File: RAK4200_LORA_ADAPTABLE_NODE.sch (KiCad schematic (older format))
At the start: 7 parts, among them U1 RAK4200

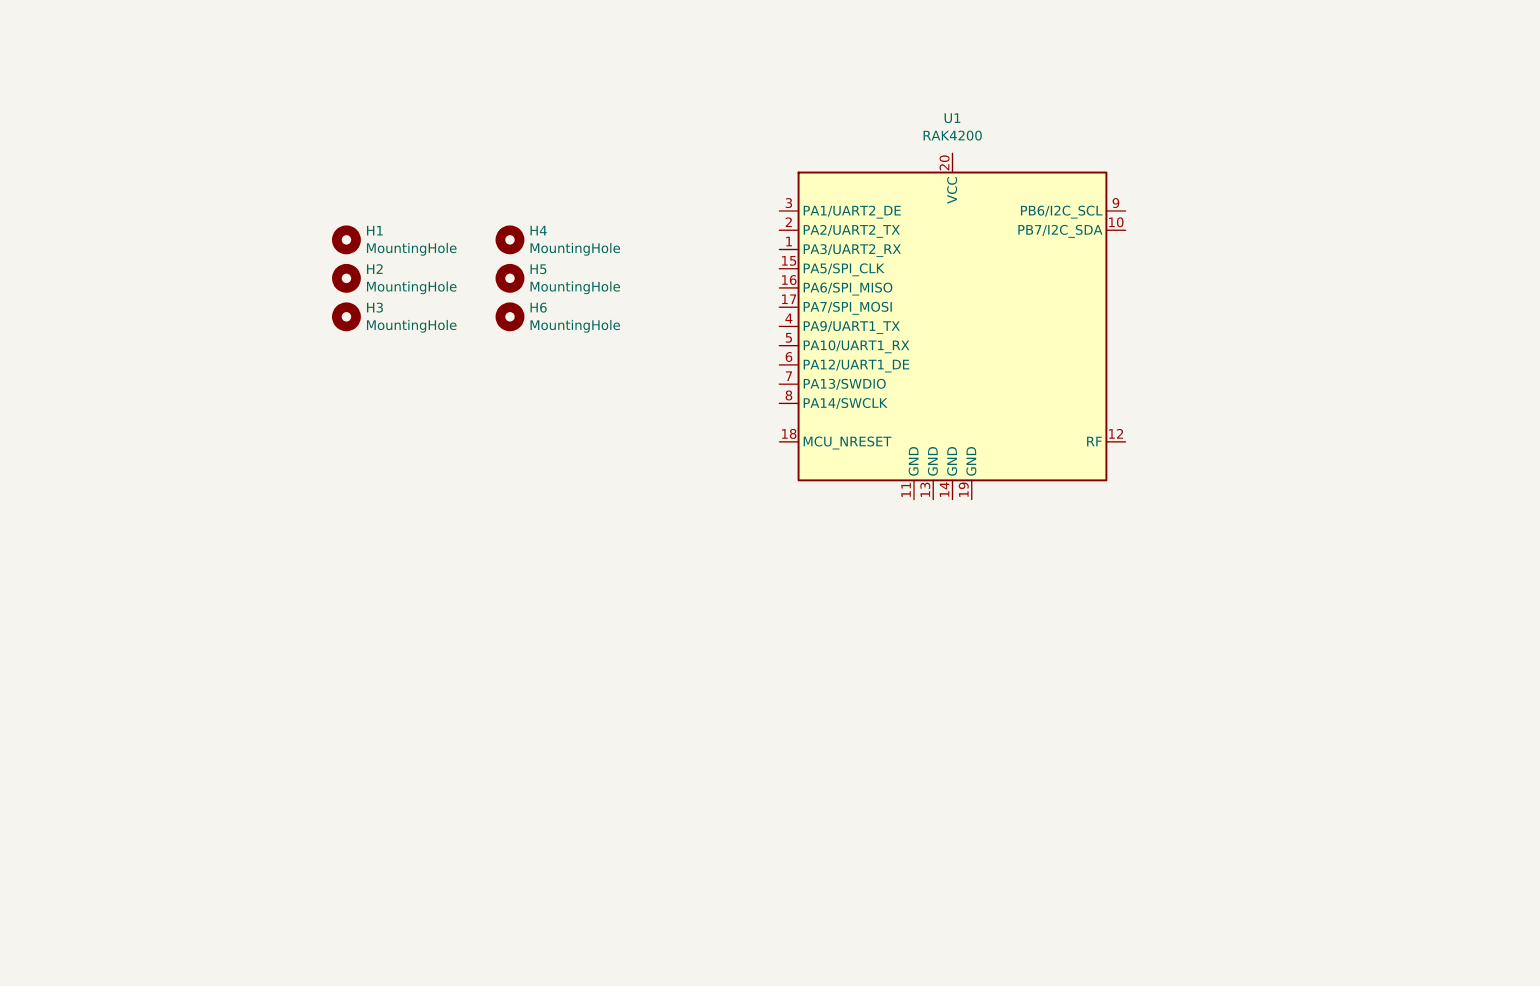
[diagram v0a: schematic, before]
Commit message: battery holder, solder jumper and screw terminal added
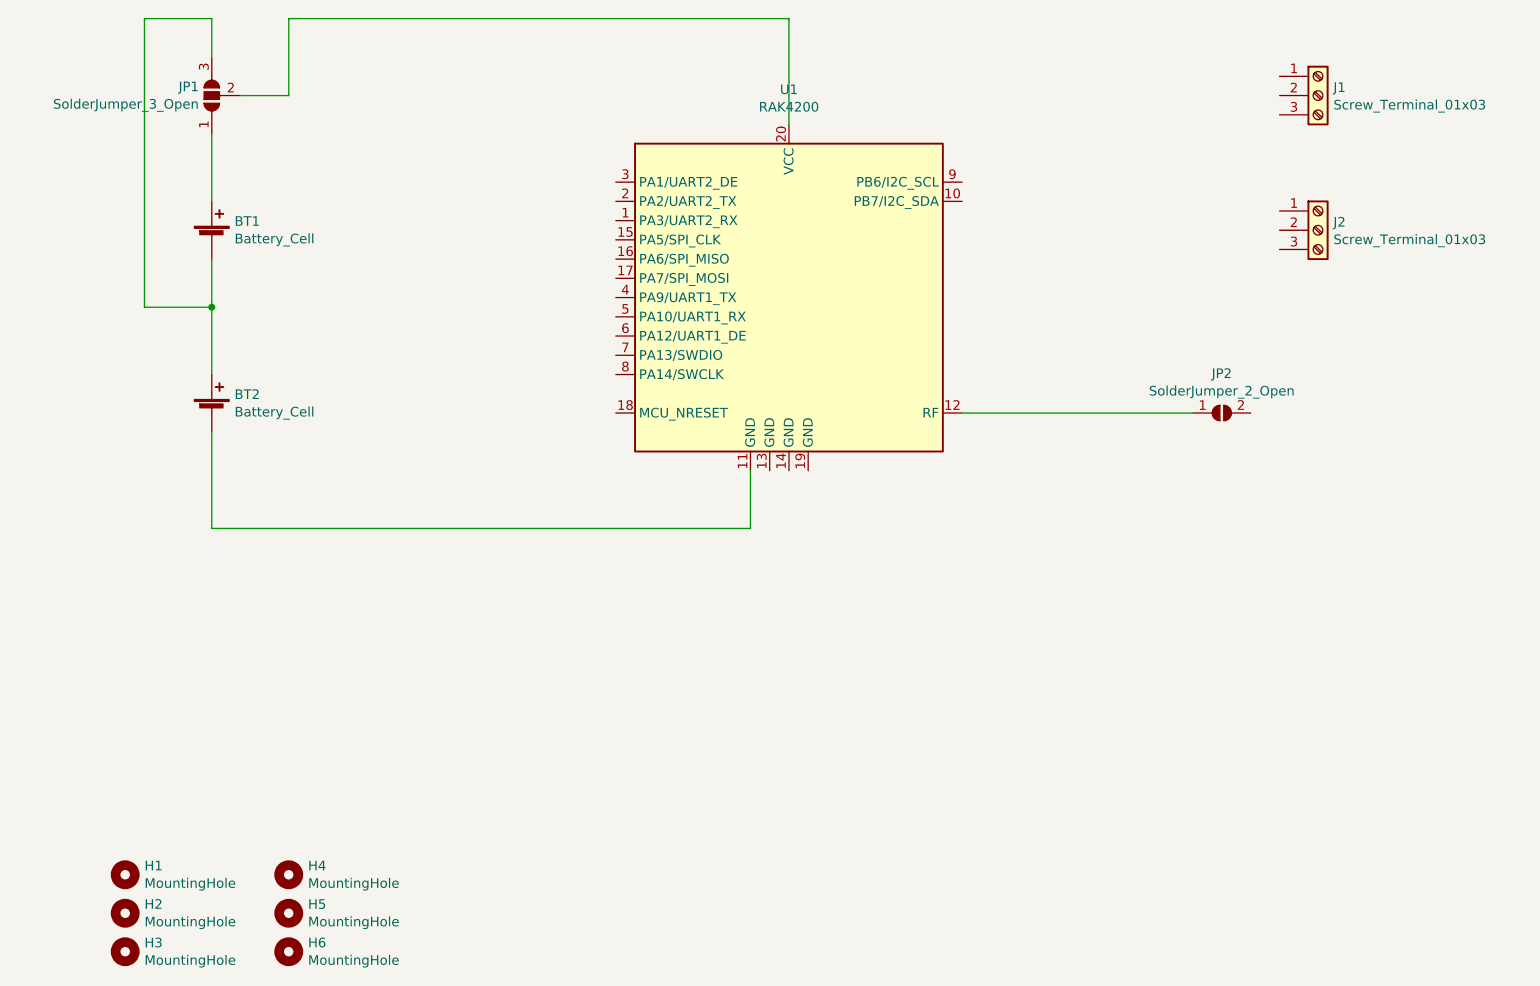
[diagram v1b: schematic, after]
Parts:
- added BT1, BT2: Battery_Cell, Battery:BatteryHolder_Keystone_2460_1xAA, symbol Device:Battery_Cell
- added J1, J2: Screw_Terminal_01x03, TerminalBlock_4Ucon:TerminalBlock_4Ucon_1x03_P3.50mm_Horizontal, symbol Connector:Screw_Terminal_01x03
- added JP1: SolderJumper_3_Open, Jumper:SolderJumper-3_P1.3mm_Open_RoundedPad1.0x1.5mm_NumberLabels, symbol Jumper:SolderJumper_3_Open
- added JP2: SolderJumper_2_Open, Jumper:SolderJumper-2_P1.3mm_Open_RoundedPad1.0x1.5mm, symbol Jumper:SolderJumper_2_Open
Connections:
- net at U1.11 (GND): now also BT2.2 (-)
- net at U1.12 (RF): now also JP2.1 (A)
- net at U1.20 (VCC): now also JP1.2 (C)
- new net: BT1.2 (-), BT2.1 (+), JP1.3 (B)
- new net: BT1.1 (+), JP1.1 (A)
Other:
- moved on the sheet: H1, H2, H3, H4, H5, H6, U1
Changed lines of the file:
@@
 L Mechanical:MountingHole H1
 U 1 1 5EED2AEB
-P 3350 3200
-F 0 "H1" H 3450 3246 50  0000 L CNN
-F 1 "MountingHole" H 3450 3155 50  0000 L CNN
-F 2 "MountingHole:MountingHole_3mm" H 3350 3200 50  0001 C CNN
-F 3 "~" H 3350 3200 50  0001 C CNN
-	1    3350 3200
+P 2200 6500
+F 0 "H1" H 2300 6546 50  0000 L CNN
+F 1 "MountingHole" H 2300 6455 50  0000 L CNN
+F 2 "MountingHole:MountingHole_3mm" H 2200 6500 50  0001 C CNN
+F 3 "~" H 2200 6500 50  0001 C CNN
+	1    2200 6500
 	1    0    0    -1
 $EndComp
@@
 L Mechanical:MountingHole H2
 U 1 1 5EED2E39
-P 3350 3400
-F 0 "H2" H 3450 3446 50  0000 L CNN
-F 1 "MountingHole" H 3450 3355 50  0000 L CNN
-F 2 "MountingHole:MountingHole_3mm" H 3350 3400 50  0001 C CNN
-F 3 "~" H 3350 3400 50  0001 C CNN
-	1    3350 3400
+P 2200 6700
+F 0 "H2" H 2300 6746 50  0000 L CNN
+F 1 "MountingHole" H 2300 6655 50  0000 L CNN
+F 2 "MountingHole:MountingHole_3mm" H 2200 6700 50  0001 C CNN
+F 3 "~" H 2200 6700 50  0001 C CNN
+	1    2200 6700
 	1    0    0    -1
 $EndComp
@@
 L Mechanical:MountingHole H3
 U 1 1 5EED3144
-P 3350 3600
-F 0 "H3" H 3450 3646 50  0000 L CNN
-F 1 "MountingHole" H 3450 3555 50  0000 L CNN
-F 2 "MountingHole:MountingHole_3mm" H 3350 3600 50  0001 C CNN
-F 3 "~" H 3350 3600 50  0001 C CNN
-	1    3350 3600
+P 2200 6900
+F 0 "H3" H 2300 6946 50  0000 L CNN
+F 1 "MountingHole" H 2300 6855 50  0000 L CNN
+F 2 "MountingHole:MountingHole_3mm" H 2200 6900 50  0001 C CNN
+F 3 "~" H 2200 6900 50  0001 C CNN
+	1    2200 6900
 	1    0    0    -1
 $EndComp
@@
 L Mechanical:MountingHole H4
 U 1 1 5EED33AC
-P 4200 3200
-F 0 "H4" H 4300 3246 50  0000 L CNN
-F 1 "MountingHole" H 4300 3155 50  0000 L CNN
-F 2 "MountingHole:MountingHole_3mm" H 4200 3200 50  0001 C CNN
-F 3 "~" H 4200 3200 50  0001 C CNN
-	1    4200 3200
+P 3050 6500
+F 0 "H4" H 3150 6546 50  0000 L CNN
+F 1 "MountingHole" H 3150 6455 50  0000 L CNN
+F 2 "MountingHole:MountingHole_3mm" H 3050 6500 50  0001 C CNN
+F 3 "~" H 3050 6500 50  0001 C CNN
+	1    3050 6500
 	1    0    0    -1
 $EndComp
@@
 L Mechanical:MountingHole H6
 U 1 1 5EED36FB
-P 4200 3600
-F 0 "H6" H 4300 3646 50  0000 L CNN
-F 1 "MountingHole" H 4300 3555 50  0000 L CNN
-F 2 "MountingHole:MountingHole_3mm" H 4200 3600 50  0001 C CNN
-F 3 "~" H 4200 3600 50  0001 C CNN
-	1    4200 3600
+P 3050 6900
+F 0 "H6" H 3150 6946 50  0000 L CNN
+F 1 "MountingHole" H 3150 6855 50  0000 L CNN
+F 2 "MountingHole:MountingHole_3mm" H 3050 6900 50  0001 C CNN
+F 3 "~" H 3050 6900 50  0001 C CNN
+	1    3050 6900
 	1    0    0    -1
 $EndComp
@@
 L Mechanical:MountingHole H5
 U 1 1 5EED3A44
-P 4200 3400
-F 0 "H5" H 4300 3446 50  0000 L CNN
-F 1 "MountingHole" H 4300 3355 50  0000 L CNN
-F 2 "MountingHole:MountingHole_3mm" H 4200 3400 50  0001 C CNN
-F 3 "~" H 4200 3400 50  0001 C CNN
-	1    4200 3400
+P 3050 6700
+F 0 "H5" H 3150 6746 50  0000 L CNN
+F 1 "MountingHole" H 3150 6655 50  0000 L CNN
+F 2 "MountingHole:MountingHole_3mm" H 3050 6700 50  0001 C CNN
+F 3 "~" H 3050 6700 50  0001 C CNN
+	1    3050 6700
 	1    0    0    -1
 $EndComp
@@
 L RF_Module:RAK4200 U1
 U 1 1 5F134DC1
-P 6500 3650
-F 0 "U1" H 6500 4731 50  0000 C CNN
-F 1 "RAK4200" H 6500 4640 50  0000 C CNN
-F 2 "RF_Module:RAK4200" H 6700 3950 50  0001 C CNN
-F 3 "https://downloads.rakwireless.com/LoRa/RAK4200/Hardware-Specification/RAK4200_Module_Specifications_V1.4.pdf" H 6700 3950 50  0001 C CNN
-	1    6500 3650
+P 5650 3500
+F 0 "U1" H 5650 4581 50  0000 C CNN
+F 1 "RAK4200" H 5650 4490 50  0000 C CNN
+F 2 "RF_Module:RAK4200" H 5850 3800 50  0001 C CNN
+F 3 "https://downloads.rakwireless.com/LoRa/RAK4200/Hardware-Specification/RAK4200_Module_Specifications_V1.4.pdf" H 5850 3800 50  0001 C CNN
+	1    5650 3500
 	1    0    0    -1
 $EndComp
+$Comp
+L Device:Battery_Cell BT2
+U 1 1 5F1A264D
+P 2650 4100
+F 0 "BT2" H 2768 4196 50  0000 L CNN
+F 1 "Battery_Cell" H 2768 4105 50  0000 L CNN
+F 2 "Battery:BatteryHolder_Keystone_2460_1xAA" V 2650 4160 50  0001 C CNN
+F 3 "~" V 2650 4160 50  0001 C CNN
+	1    2650 4100
+	1    0    0    -1
+$EndComp
+$Comp
+L Device:Battery_Cell BT1
+U 1 1 5F1A2EE6
+P 2650 3200
+F 0 "BT1" H 2768 3296 50  0000 L CNN
+F 1 "Battery_Cell" H 2768 3205 50  0000 L CNN
+F 2 "Battery:BatteryHolder_Keystone_2460_1xAA" V 2650 3260 50  0001 C CNN
+F 3 "~" V 2650 3260 50  0001 C CNN
+	1    2650 3200
+	1    0    0    -1
+$EndComp
+$Comp
+L Jumper:SolderJumper_3_Open JP1
+U 1 1 5F1A44C5
+P 2650 2450
+F 0 "JP1" V 2696 2517 50  0000 L CNN
+F 1 "SolderJumper_3_Open" V 2605 2517 50  0000 L CNN
+F 2 "Jumper:SolderJumper-3_P1.3mm_Open_RoundedPad1.0x1.5mm_NumberLabels" H 2650 2450 50  0001 C CNN
+F 3 "~" H 2650 2450 50  0001 C CNN
+	1    2650 2450
+	0    -1   -1   0
+$EndComp
+$Comp
+L Connector:Screw_Terminal_01x03 J1
+U 1 1 5F1A6EDA
+P 8400 2450
+F 0 "J1" H 8480 2492 50  0000 L CNN
+F 1 "Screw_Terminal_01x03" H 8480 2401 50  0000 L CNN
+F 2 "TerminalBlock_4Ucon:TerminalBlock_4Ucon_1x03_P3.50mm_Horizontal" H 8400 2450 50  0001 C CNN
+F 3 "~" H 8400 2450 50  0001 C CNN
+	1    8400 2450
+	1    0    0    -1
+$EndComp
+$Comp
+L Connector:Screw_Terminal_01x03 J2
+U 1 1 5F1A74A2
+P 8400 3150
+F 0 "J2" H 8480 3192 50  0000 L CNN
+F 1 "Screw_Terminal_01x03" H 8480 3101 50  0000 L CNN
+F 2 "TerminalBlock_4Ucon:TerminalBlock_4Ucon_1x03_P3.50mm_Horizontal" H 8400 3150 50  0001 C CNN
+F 3 "~" H 8400 3150 50  0001 C CNN
+	1    8400 3150
+	1    0    0    -1
+$EndComp
+$Comp
+L Jumper:SolderJumper_2_Open JP2
+U 1 1 5F1A7BAB
+P 7900 4100
+F 0 "JP2" H 7900 4305 50  0000 C CNN
+F 1 "SolderJumper_2_Open" H 7900 4214 50  0000 C CNN
+F 2 "Jumper:SolderJumper-2_P1.3mm_Open_RoundedPad1.0x1.5mm" H 7900 4100 50  0001 C CNN
+F 3 "~" H 7900 4100 50  0001 C CNN
+	1    7900 4100
+	1    0    0    -1
+$EndComp
+Wire Wire Line
+	2650 3300 2650 3550
+Wire Wire Line
+	2650 4200 2650 4700
+Wire Wire Line
+	2650 4700 5450 4700
+Wire Wire Line
+	5450 4700 5450 4400
+Wire Wire Line
+	2800 2450 3050 2450
+Wire Wire Line
+	3050 2450 3050 2050
+Wire Wire Line
+	3050 2050 5650 2050
+Wire Wire Line
+	5650 2050 5650 2600
+Wire Wire Line
+	2650 3000 2650 2650
+Wire Wire Line
+	2650 2250 2650 2050
+Wire Wire Line
+	2650 2050 2300 2050
+Wire Wire Line
+	2300 2050 2300 3550
+Wire Wire Line
+	2300 3550 2650 3550
+Connection ~ 2650 3550
+Wire Wire Line
+	2650 3550 2650 3900
+Wire Wire Line
+	6550 4100 7750 4100
 $EndSCHEMATC

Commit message: expansion connectors added
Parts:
- removed H1, H6: MountingHole, MountingHole:MountingHole_3mm, symbol Mechanical:MountingHole
- added J3, J4: Conn_01x11_Male, Connector_PinHeader_2.54mm:PinHeader_1x11_P2.54mm_Vertical, symbol Connector:Conn_01x11_Male
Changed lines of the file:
@@
 $EndDescr
-$Comp
-L Mechanical:MountingHole H1
-U 1 1 5EED2AEB
-P 2200 6500
-F 0 "H1" H 2300 6546 50  0000 L CNN
-F 1 "MountingHole" H 2300 6455 50  0000 L CNN
-F 2 "MountingHole:MountingHole_3mm" H 2200 6500 50  0001 C CNN
-F 3 "~" H 2200 6500 50  0001 C CNN
-	1    2200 6500
-	1    0    0    -1
-$EndComp
 $Comp
 L Mechanical:MountingHole H2
@@
 F 3 "~" H 3050 6500 50  0001 C CNN
 	1    3050 6500
-	1    0    0    -1
-$EndComp
-$Comp
-L Mechanical:MountingHole H6
-U 1 1 5EED36FB
-P 3050 6900
-F 0 "H6" H 3150 6946 50  0000 L CNN
-F 1 "MountingHole" H 3150 6855 50  0000 L CNN
-F 2 "MountingHole:MountingHole_3mm" H 3050 6900 50  0001 C CNN
-F 3 "~" H 3050 6900 50  0001 C CNN
-	1    3050 6900
 	1    0    0    -1
 $EndComp
@@
 Wire Wire Line
 	6550 4100 7750 4100
+$Comp
+L Connector:Conn_01x11_Male J3
+U 1 1 5F1C2DB6
+P 3500 3450
+F 0 "J3" H 3608 4131 50  0000 C CNN
+F 1 "Conn_01x11_Male" H 3608 4040 50  0000 C CNN
+F 2 "Connector_PinHeader_2.54mm:PinHeader_1x11_P2.54mm_Vertical" H 3500 3450 50  0001 C CNN
+F 3 "~" H 3500 3450 50  0001 C CNN
+	1    3500 3450
+	1    0    0    -1
+$EndComp
+$Comp
+L Connector:Conn_01x11_Male J4
+U 1 1 5F1CF9D8
+P 7450 3450
+F 0 "J4" H 7422 3474 50  0000 R CNN
+F 1 "Conn_01x11_Male" H 7422 3383 50  0000 R CNN
+F 2 "Connector_PinHeader_2.54mm:PinHeader_1x11_P2.54mm_Vertical" H 7450 3450 50  0001 C CNN
+F 3 "~" H 7450 3450 50  0001 C CNN
+	1    7450 3450
+	-1   0    0    -1
+$EndComp
 $EndSCHEMATC
